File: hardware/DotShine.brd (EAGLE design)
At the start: 30 x 65 mm, 57 parts, among them CN1 1X4-BIG, IC1 CAT24M010TS, IC3 SI1145, J3 USB-MICROB, U1 ATMEGA328P-MU-QFN32, U2 TMP102, U3 ATSHA204-TSU, X2 MC-RTC-RV-4162-C7-I2C, X3 S4B-ZR

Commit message: Sync
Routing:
- net +5V: track 51.3 -> 50.5 mm
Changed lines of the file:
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@@
 <wire x1="8.51" y1="50.65" x2="8.14" y2="51.02" width="0.3048" layer="1"/>
 <contactref element="D5" pad="C"/>
-<wire x1="4.296" y1="33.96" x2="4.296" y2="33.181" width="0.3048" layer="1"/>
 <contactref element="D4" pad="C"/>
 <wire x1="18.17235" y1="58.956671875" x2="15.116271875" y2="58.956671875" width="0.3048" layer="1"/>

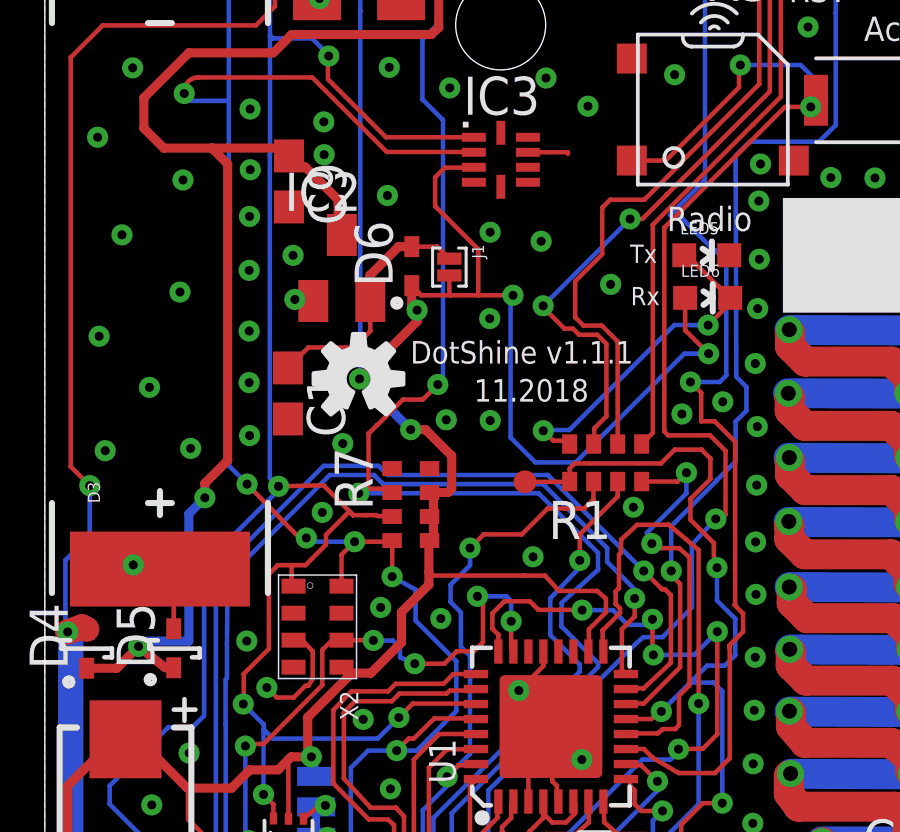
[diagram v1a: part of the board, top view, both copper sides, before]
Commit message: Add UV Sensor INT to cabled OR
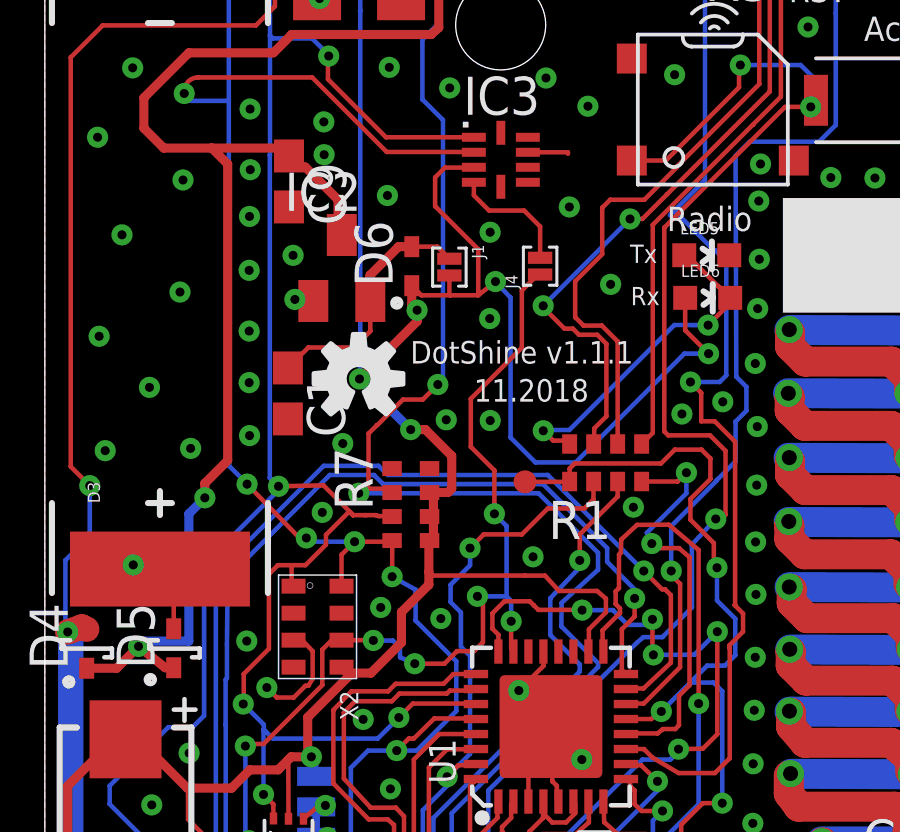
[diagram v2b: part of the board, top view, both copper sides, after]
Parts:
- added J4: (no value), solderjumper:2.MED
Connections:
- removed net CS_FLASH: U1.23, U2.3, X2.P$6
- new net N$33: IC3.4, J4.2
- net INT_MULTIPLE: now also J4.1, U1.23, U2.3, X2.P$6; no longer IC3.4
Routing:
- net INT_MULTIPLE: track 0.00 -> 33.6 mm, vias 0 -> 7
- net CS_FLASH: track 21.0 -> 0.00 mm, vias 6 -> 0
- net N$33: track 0.00 -> 4.12 mm
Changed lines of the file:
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@@
 <element name="LED7" library="SparkFun" package="LED-0603" value="" x="15.9004" y="61.722"/>
 <element name="J2" library="solderjumper" package="2.MED" value="" x="20.1422" y="22.225" rot="R270"/>
+<element name="J4" library="solderjumper" package="2.MED" value="" x="16.51" y="47.3456" rot="R90"/>
 </elements>
 <signals>
@@
 <via x="3.487859375" y="43.305615625" extent="1-16" drill="0.3"/>
 <via x="18.102859375" y="52.677615625" extent="1-16" drill="0.3"/>
-<via x="16.544859375" y="48.176615625" extent="1-16" drill="0.3"/>
+<via x="17.484659375" y="49.319615625" extent="1-16" drill="0.3"/>
 <via x="16.706859375" y="53.617615625" extent="1-16" drill="0.3"/>
 <via x="11.419859375" y="49.701615625" extent="1-16" drill="0.3"/>
@@
 <wire x1="16.355" y1="40.805" x2="15.525" y2="41.635" width="0.1524" layer="16"/>
 <wire x1="15.525" y1="41.635" x2="15.525" y2="46.295" width="0.1524" layer="16"/>
-<wire x1="15.525" y1="46.295" x2="15.605" y2="46.375" width="0.1524" layer="16"/>
-<via x="15.605" y="46.375" extent="1-16" drill="0.3"/>
-<wire x1="15.605" y1="46.375" x2="14.448" y2="46.375" width="0.1524" layer="1"/>
+<wire x1="15.525" y1="46.295" x2="15.0208" y2="46.8322" width="0.1524" layer="16"/>
+<via x="15.0208" y="46.8322" extent="1-16" drill="0.3"/>
+<wire x1="15.0208" y1="46.8322" x2="14.448" y2="46.375" width="0.1524" layer="1"/>
 <contactref element="LED6" pad="A"/>
 <wire x1="14.448" y1="46.375" x2="13.517" y2="46.375" width="0.1524" layer="1"/>
@@
 <wire x1="25.805384375" y1="25.76285" x2="25.77185625" y2="26.057353125" width="0" layer="19" extent="1-1"/>
 </signal>
-<signal name="CS_FLASH">
-<contactref element="U1" pad="23"/>
-<wire x1="15.5448" y1="35.5092" x2="15.5448" y2="34.5948" width="0.1524" layer="1"/>
-<wire x1="15.5448" y1="34.5948" x2="15.62" y2="34.5" width="0.1524" layer="1"/>
-<via x="15.5448" y="35.5092" extent="1-16" drill="0.3"/>
-<contactref element="X2" pad="P$6"/>
-<wire x1="9.89" y1="34.88" x2="10.94" y2="34.88" width="0.1524" layer="1"/>
-<wire x1="10.94" y1="34.88" x2="10.95" y2="34.87" width="0.1524" layer="1"/>
-<via x="10.95" y="34.87" extent="1-16" drill="0.3"/>
-<wire x1="10.95" y1="34.87" x2="11.6" y2="34.865" width="0.1524" layer="16"/>
-<wire x1="11.6" y1="34.865" x2="11.84" y2="34.635" width="0.1524" layer="16"/>
-<wire x1="11.84" y1="34.635" x2="11.84" y2="34.31" width="0.1524" layer="16"/>
-<wire x1="11.84" y1="34.31" x2="12.33" y2="34.095" width="0.1524" layer="16"/>
-<via x="12.33" y="34.095" extent="1-16" drill="0.3"/>
-<wire x1="12.33" y1="34.095" x2="12.075" y2="34.095" width="0.1524" layer="1"/>
-<wire x1="12.33" y1="34.095" x2="13.32" y2="34.095" width="0.1524" layer="1"/>
-<wire x1="13.32" y1="34.095" x2="13.74" y2="34.515" width="0.1524" layer="1"/>
-<wire x1="13.74" y1="34.515" x2="14.31" y2="34.515" width="0.1524" layer="1"/>
-<wire x1="14.31" y1="34.515" x2="14.605" y2="34.81" width="0.1524" layer="1"/>
-<wire x1="14.605" y1="34.81" x2="14.605" y2="36.155" width="0.1524" layer="1"/>
-<wire x1="14.605" y1="36.155" x2="14.42" y2="36.34" width="0.1524" layer="1"/>
-<via x="14.42" y="36.34" extent="1-16" drill="0.3"/>
-<wire x1="14.42" y1="36.34" x2="15.3898" y2="36.34" width="0.1524" layer="16"/>
-<contactref element="U2" pad="3"/>
-<wire x1="8.62156875" y1="27.605871875" x2="8.61656875" y2="27.91343125" width="0.1524" layer="1"/>
-<wire x1="8.61656875" y1="27.91343125" x2="8.335" y2="28.195" width="0.1524" layer="1"/>
-<via x="6.685" y="31.35" extent="1-16" drill="0.3"/>
-<wire x1="6.685" y1="31.35" x2="6.685" y2="28.31" width="0.1524" layer="16"/>
-<wire x1="6.685" y1="28.31" x2="6.8" y2="28.195" width="0.1524" layer="16"/>
-<via x="6.8" y="28.195" extent="1-16" drill="0.3"/>
-<wire x1="6.8" y1="28.195" x2="8.335" y2="28.195" width="0.1524" layer="1"/>
-<wire x1="15.3898" y1="36.34" x2="15.5448" y2="36.185" width="0.1524" layer="16"/>
-<wire x1="15.5448" y1="36.185" x2="15.5448" y2="35.5092" width="0.1524" layer="16"/>
-<wire x1="9.25" y1="34.564" x2="9.25" y2="33.382" width="0.1524" layer="1"/>
-<wire x1="9.25" y1="33.382" x2="7.292" y2="31.419" width="0.1524" layer="1"/>
-<wire x1="7.292" y1="31.419" x2="6.754" y2="31.419" width="0.1524" layer="1"/>
-<wire x1="6.754" y1="31.419" x2="6.685" y2="31.35" width="0.1524" layer="1"/>
-<wire x1="9.271" y1="34.574" x2="9.577" y2="34.88" width="0.1524" layer="1"/>
-<wire x1="9.577" y1="34.88" x2="9.89" y2="34.88" width="0.1524" layer="1"/>
-<wire x1="9.25" y1="34.564" x2="9.271" y2="34.574" width="0" layer="19" extent="1-1"/>
-</signal>
 <signal name="N$13">
 <contactref element="R1" pad="8"/>
@@
 <wire x1="2.9464" y1="37.3888" x2="3.0852" y2="37.25" width="0.1524" layer="1"/>
 <wire x1="3.0852" y1="37.25" x2="3.837" y2="37.25" width="0.1524" layer="1"/>
-</signal>
-<signal name="INT_MULTIPLE">
-<contactref element="IC3" pad="4"/>
 </signal>
 <signal name="N$25">
@@
 <wire x1="12.1412" y1="60.706" x2="11.8872" y2="60.96" width="0.1524" layer="16"/>
 </signal>
+<signal name="N$33">
+<contactref element="IC3" pad="4"/>
+<contactref element="J4" pad="2"/>
+<wire x1="14.301" y1="50.142" x2="14.301" y2="49.707" width="0.1524" layer="1"/>
+<wire x1="14.301" y1="49.707" x2="14.8082" y2="49.1998" width="0.1524" layer="1"/>
+<wire x1="14.8082" y1="49.1998" x2="15.9766" y2="49.1998" width="0.1524" layer="1"/>
+<wire x1="15.9766" y1="49.1998" x2="16.51" y2="48.6664" width="0.1524" layer="1"/>
+<wire x1="16.51" y1="48.6664" x2="16.51" y2="47.625" width="0.1524" layer="1"/>
+</signal>
+<signal name="INT_MULTIPLE">
+<contactref element="J4" pad="1"/>
+<contactref element="X2" pad="P$6"/>
+<wire x1="9.577" y1="34.88" x2="9.89" y2="34.88" width="0.1524" layer="1"/>
+<contactref element="U2" pad="3"/>
+<wire x1="8.62156875" y1="27.605871875" x2="8.61656875" y2="27.91343125" width="0.1524" layer="1"/>
+<wire x1="8.61656875" y1="27.91343125" x2="8.335" y2="28.195" width="0.1524" layer="1"/>
+<via x="6.685" y="31.35" extent="1-16" drill="0.3"/>
+<wire x1="6.685" y1="31.35" x2="6.685" y2="28.31" width="0.1524" layer="16"/>
+<wire x1="6.685" y1="28.31" x2="6.8" y2="28.195" width="0.1524" layer="16"/>
+<via x="6.8" y="28.195" extent="1-16" drill="0.3"/>
+<wire x1="6.8" y1="28.195" x2="8.335" y2="28.195" width="0.1524" layer="1"/>
+<wire x1="9.25" y1="34.564" x2="9.25" y2="33.382" width="0.1524" layer="1"/>
+<wire x1="9.25" y1="33.382" x2="7.292" y2="31.419" width="0.1524" layer="1"/>
+<wire x1="7.292" y1="31.419" x2="6.754" y2="31.419" width="0.1524" layer="1"/>
+<wire x1="6.754" y1="31.419" x2="6.685" y2="31.35" width="0.1524" layer="1"/>
+<wire x1="9.89" y1="34.88" x2="9.566" y2="34.88" width="0.1524" layer="1"/>
+<wire x1="9.566" y1="34.88" x2="9.25" y2="34.564" width="0.1524" layer="1"/>
+<contactref element="U1" pad="23"/>
+<wire x1="15.5448" y1="35.5092" x2="15.5448" y2="34.5948" width="0.1524" layer="1"/>
+<wire x1="15.5448" y1="34.5948" x2="15.62" y2="34.5" width="0.1524" layer="1"/>
+<via x="15.5448" y="35.5092" extent="1-16" drill="0.3"/>
+<wire x1="10.94" y1="34.88" x2="10.95" y2="34.87" width="0.1524" layer="1"/>
+<via x="10.95" y="34.87" extent="1-16" drill="0.3"/>
+<wire x1="10.95" y1="34.87" x2="11.6" y2="34.865" width="0.1524" layer="16"/>
+<wire x1="11.6" y1="34.865" x2="11.84" y2="34.635" width="0.1524" layer="16"/>
+<wire x1="11.84" y1="34.635" x2="11.84" y2="34.31" width="0.1524" layer="16"/>
+<wire x1="11.84" y1="34.31" x2="12.33" y2="34.095" width="0.1524" layer="16"/>
+<via x="12.33" y="34.095" extent="1-16" drill="0.3"/>
+<wire x1="12.33" y1="34.095" x2="12.075" y2="34.095" width="0.1524" layer="1"/>
+<wire x1="12.33" y1="34.095" x2="13.32" y2="34.095" width="0.1524" layer="1"/>
+<wire x1="13.32" y1="34.095" x2="13.74" y2="34.515" width="0.1524" layer="1"/>
+<wire x1="13.74" y1="34.515" x2="14.31" y2="34.515" width="0.1524" layer="1"/>
+<wire x1="14.31" y1="34.515" x2="14.605" y2="34.81" width="0.1524" layer="1"/>
+<wire x1="14.605" y1="34.81" x2="14.605" y2="36.155" width="0.1524" layer="1"/>
+<wire x1="14.605" y1="36.155" x2="14.42" y2="36.34" width="0.1524" layer="1"/>
+<via x="14.42" y="36.34" extent="1-16" drill="0.3"/>
+<wire x1="14.42" y1="36.34" x2="15.3898" y2="36.34" width="0.1524" layer="16"/>
+<wire x1="15.3898" y1="36.34" x2="15.5448" y2="36.185" width="0.1524" layer="16"/>
+<wire x1="15.5448" y1="36.185" x2="15.5448" y2="35.5092" width="0.1524" layer="16"/>
+<wire x1="10.94" y1="34.88" x2="9.89" y2="34.88" width="0.1524" layer="1"/>
+<wire x1="15.3898" y1="36.34" x2="15.3898" y2="38.6868" width="0.1524" layer="16"/>
+<wire x1="15.3898" y1="38.6868" x2="14.986" y2="39.0906" width="0.1524" layer="16"/>
+<via x="14.986" y="39.0906" extent="1-16" drill="0.3"/>
+<wire x1="14.986" y1="39.0906" x2="14.986" y2="40.5384" width="0.1524" layer="1"/>
+<wire x1="14.986" y1="40.5384" x2="14.1986" y2="41.3258" width="0.1524" layer="1"/>
+<wire x1="14.1986" y1="41.3258" x2="14.1986" y2="42.926" width="0.1524" layer="1"/>
+<wire x1="14.1986" y1="42.926" x2="15.9004" y2="44.6278" width="0.1524" layer="1"/>
+<wire x1="16.51" y1="47.0662" x2="16.4338" y2="47.0662" width="0.1524" layer="1"/>
+<wire x1="16.4338" y1="47.0662" x2="15.9004" y2="46.5328" width="0.1524" layer="1"/>
+<wire x1="15.9004" y1="46.5328" x2="15.9004" y2="44.6278" width="0.1524" layer="1"/>
+</signal>
 </signals>

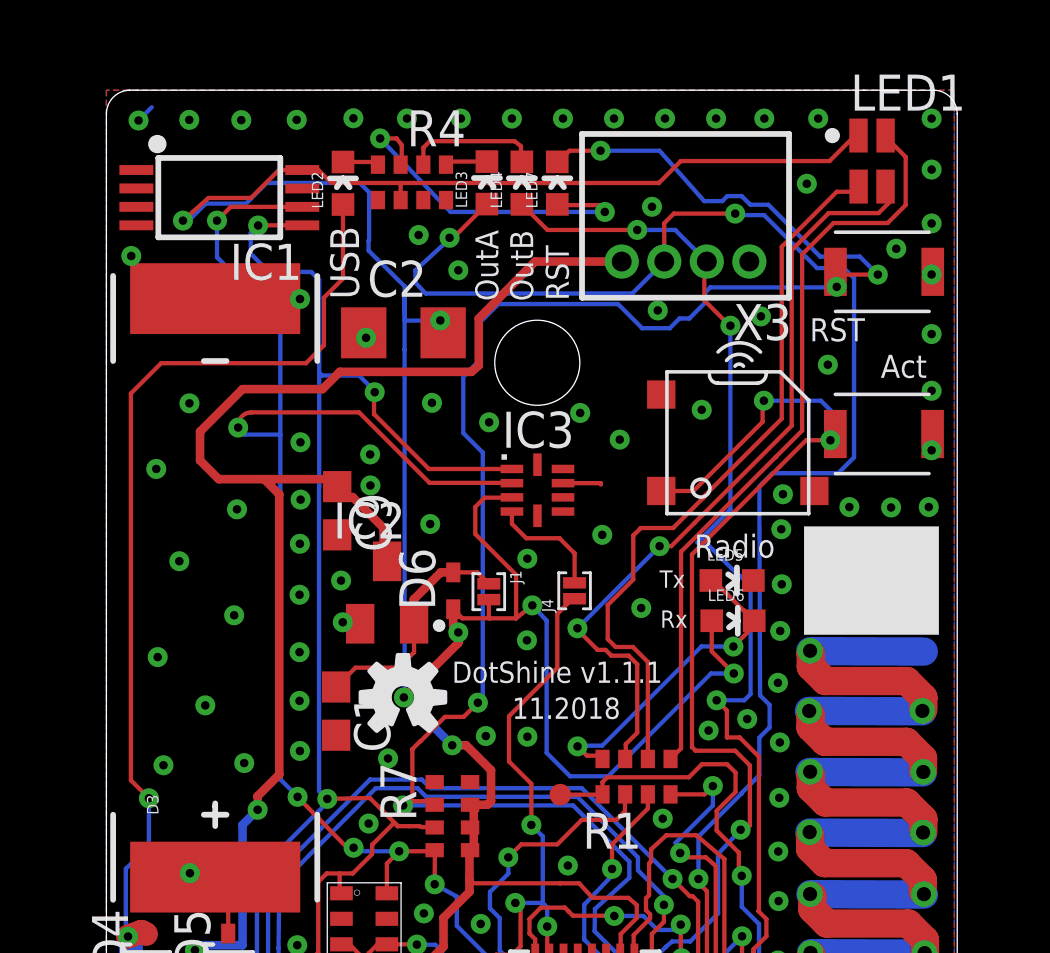
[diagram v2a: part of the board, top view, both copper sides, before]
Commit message: UV power controlled from MCU (no sleep), TXD to JST
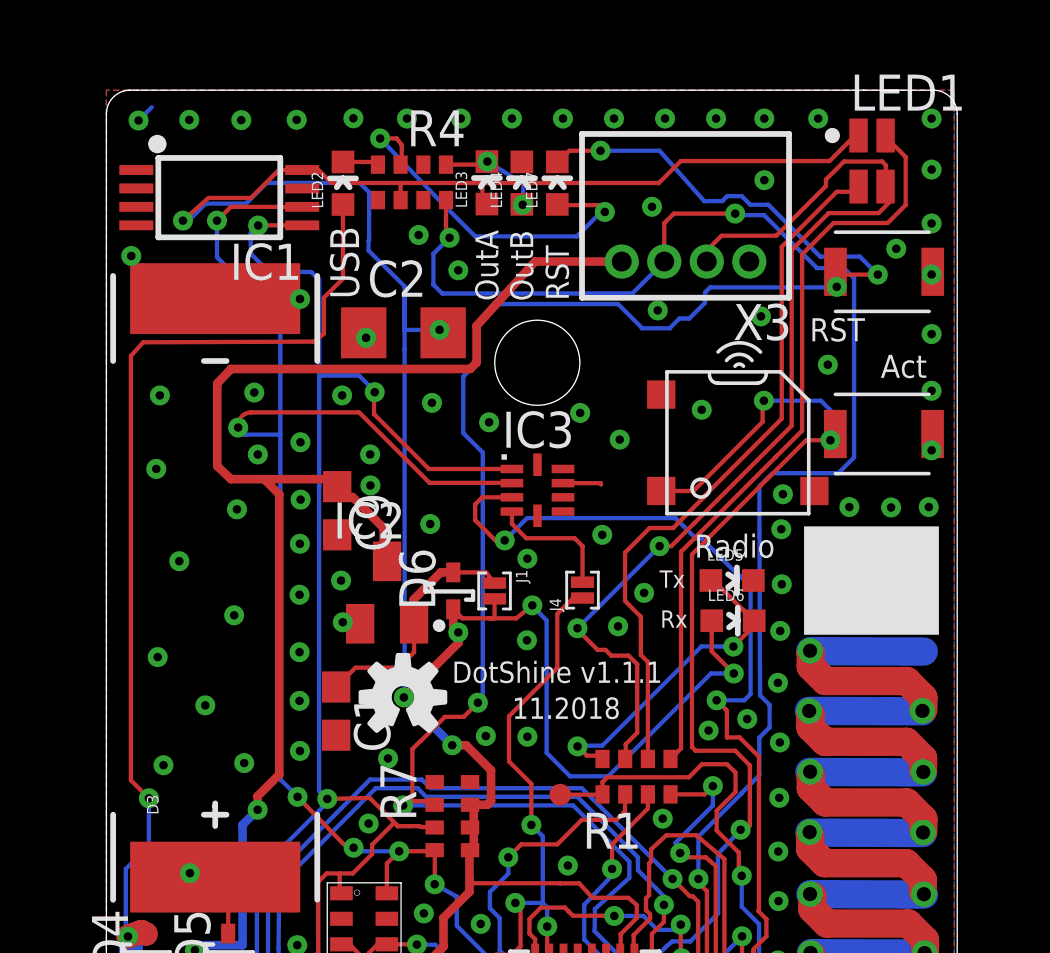
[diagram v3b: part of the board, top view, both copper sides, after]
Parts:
- moved J4 0.28 mm to (16.8, 47.4)
- moved J1 0.20 mm to (13.7, 47.3)
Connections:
- removed net N$1: LED1.3, R1.7
- removed net N$2: LED3.C, R4.1
- removed net OUTA: LED3.A, U1.14, X3.3
- removed net OUTB: LED4.A, U1.11, X3.2
- new net OUTAB: R4.8, U1.14, X3.3
- new net TXD_OUT: LED1.3, R1.7, X3.2
- new net UV_ON: IC3.3, U1.11
- net +3V3: now also LED3.A; no longer IC3.3
- net GND: now also LED4.C; no longer R4.7, R4.8
- net N$9: now also LED3.C, LED4.A, R4.1; no longer LED4.C, R4.2
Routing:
- net OUTA: track 53.2 -> 0.00 mm, vias 3 -> 0
- net OUTAB: track 0.00 -> 52.0 mm, vias 0 -> 3
- net OUTB: track 43.4 -> 0.00 mm, vias 3 -> 0
- net TXD_OUT: track 0.00 -> 36.6 mm, vias 0 -> 2
- net UV_ON: track 0.00 -> 36.0 mm, vias 0 -> 2
- net N$1: track 27.7 -> 0.00 mm, vias 2 -> 0
- net +3V3: track 228.1 -> 223.6 mm
- net N$2: track 1.49 -> 0.00 mm
- net N$4: track 26.1 -> 25.1 mm
- net N$10: track 12.4 -> 13.1 mm
- net USB_FOR_LED: track 68.5 -> 69.1 mm
- net N$9: track 4.83 -> 4.53 mm, vias 0 -> 2
- net GND: vias 144 -> 148
